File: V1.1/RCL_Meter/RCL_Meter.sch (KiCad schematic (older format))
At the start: 12 parts

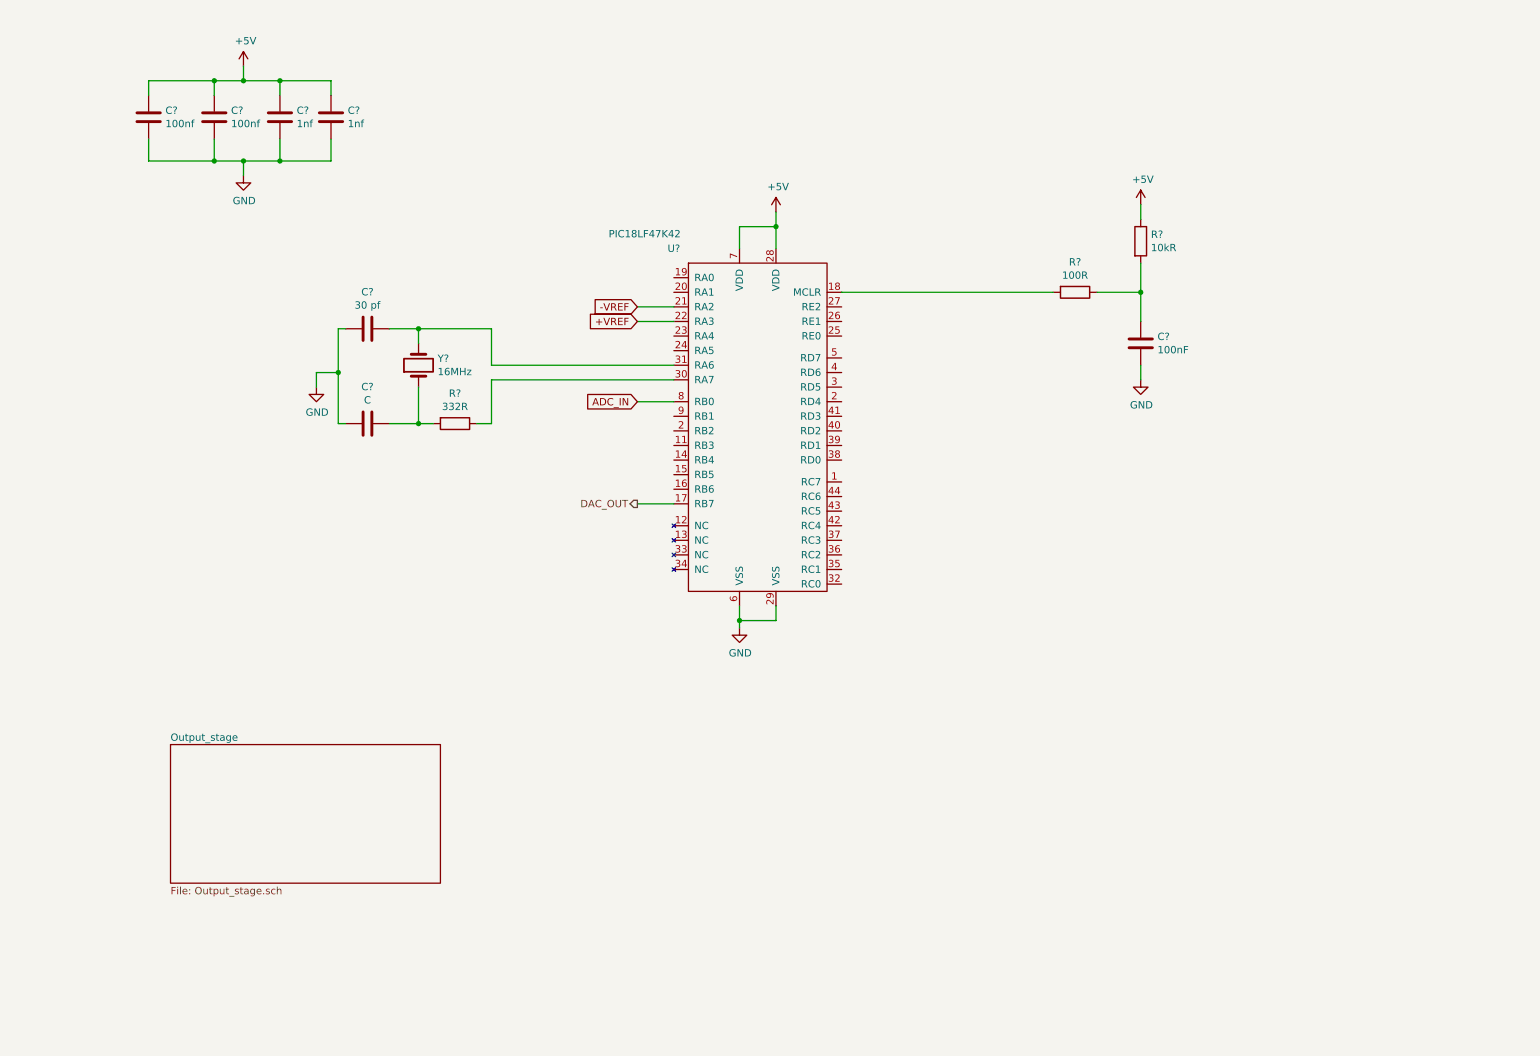
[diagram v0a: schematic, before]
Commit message: Added voltage and current front end
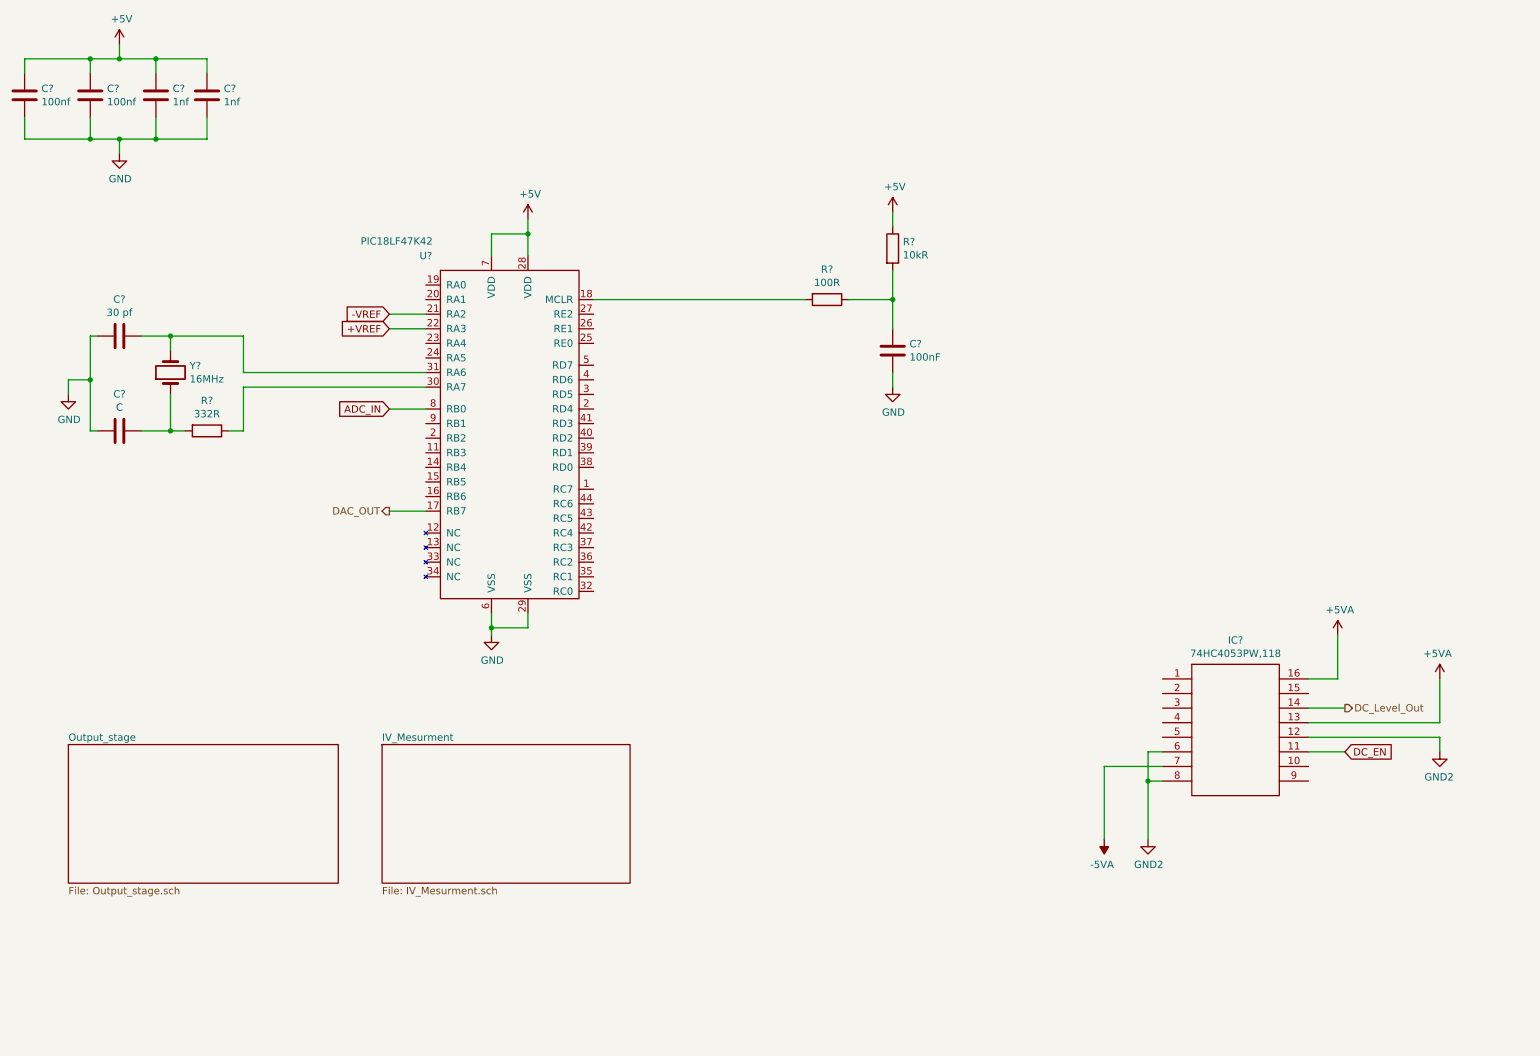
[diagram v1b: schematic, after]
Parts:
- added IC?: 74HC4053PW,118, SOP65P640X110-16N, symbol 74HC4053PW_118:74HC4053PW,118
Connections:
- new net +5VA: IC?.13, IC?.16
- new net -5VA: IC?.7
- new net DC_EN: IC?.11
- new net DC_Level_Out: IC?.14
- new net GND2: IC?.12, IC?.6, IC?.8
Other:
- moved on the sheet: C?, R?, U?, Y?

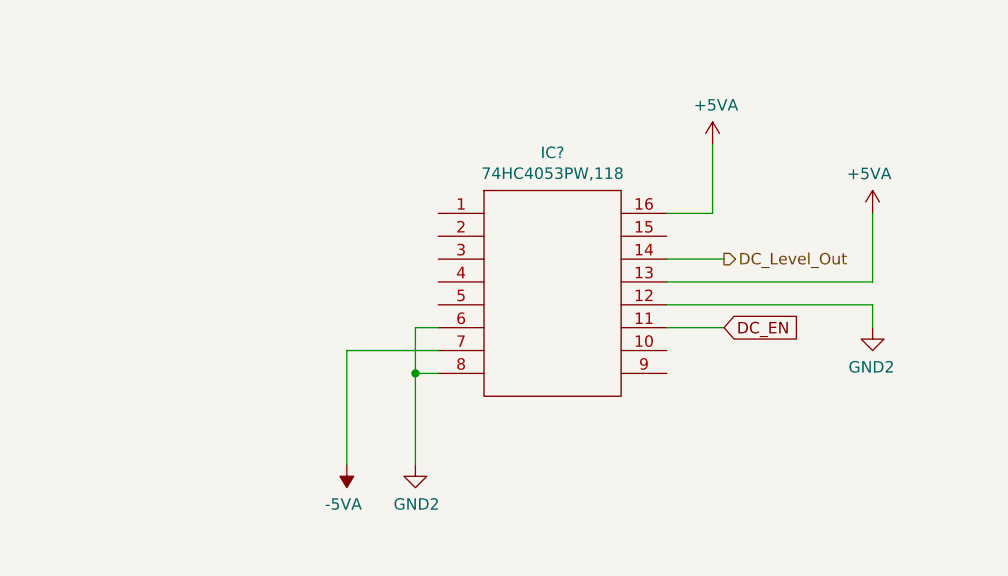
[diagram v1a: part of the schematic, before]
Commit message: added a PGA amplifier to instrumentation amplifier output
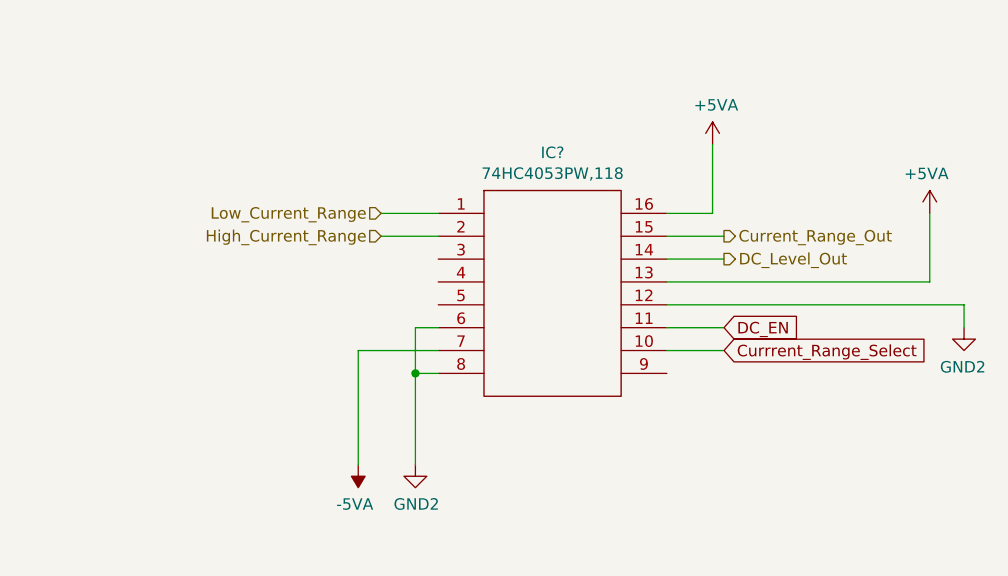
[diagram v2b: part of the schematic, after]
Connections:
- net Low_Current_Range: now reaches IC?.1
- net Currrent_Range_Select: now reaches IC?.10
- net Current_Range_Out: now reaches IC?.15
- net High_Current_Range: now reaches IC?.2
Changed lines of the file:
@@
 L power:-5VA #PWR?
 U 1 1 5F447F99
-P 8250 6200
-F 0 "#PWR?" H 8250 6300 50  0001 C CNN
-F 1 "-5VA" H 8265 6373 50  0000 C CNN
-F 2 "" H 8250 6200 50  0001 C CNN
-F 3 "" H 8250 6200 50  0001 C CNN
-	1    8250 6200
+P 8300 6200
+F 0 "#PWR?" H 8300 6300 50  0001 C CNN
+F 1 "-5VA" H 8315 6373 50  0000 C CNN
+F 2 "" H 8300 6200 50  0001 C CNN
+F 3 "" H 8300 6200 50  0001 C CNN
+	1    8300 6200
 	-1   0    0    1
 $EndComp
 Wire Wire Line
-	8250 6200 8250 5700
+	8300 6200 8300 5700
 Wire Wire Line
-	8250 5700 8650 5700
+	8300 5700 8650 5700
 Wire Wire Line
 	8550 5800 8550 5600
@@
 Connection ~ 8550 5800
 Wire Wire Line
-	10550 5400 10550 5100
+	10800 5400 10800 5100
 $Comp
 L power:+5VA #PWR?
 U 1 1 5F447FA5
-P 10550 5100
-F 0 "#PWR?" H 10550 4950 50  0001 C CNN
-F 1 "+5VA" H 10565 5273 50  0000 C CNN
-F 2 "" H 10550 5100 50  0001 C CNN
-F 3 "" H 10550 5100 50  0001 C CNN
-	1    10550 5100
+P 10800 5100
+F 0 "#PWR?" H 10800 4950 50  0001 C CNN
+F 1 "+5VA" H 10815 5273 50  0000 C CNN
+F 2 "" H 10800 5100 50  0001 C CNN
+F 3 "" H 10800 5100 50  0001 C CNN
+	1    10800 5100
 	-1   0    0    -1
 $EndComp
@@
 L power:GND2 #PWR?
 U 1 1 5F447FAB
-P 10550 5600
-F 0 "#PWR?" H 10550 5350 50  0001 C CNN
-F 1 "GND2" H 10555 5427 50  0000 C CNN
-F 2 "" H 10550 5600 50  0001 C CNN
-F 3 "" H 10550 5600 50  0001 C CNN
-	1    10550 5600
+P 10950 5600
+F 0 "#PWR?" H 10950 5350 50  0001 C CNN
+F 1 "GND2" H 10955 5427 50  0000 C CNN
+F 2 "" H 10950 5600 50  0001 C CNN
+F 3 "" H 10950 5600 50  0001 C CNN
+	1    10950 5600
 	-1   0    0    -1
 $EndComp
 Wire Wire Line
-	10550 5500 10550 5600
+	10950 5500 10950 5600
 Text GLabel 9900 5600 2    50   Input ~ 0
 DC_EN
@@
 Wire Wire Line
 	9900 5300 9650 5300
-Wire Wire Line
-	9650 5400 10550 5400
-Wire Wire Line
-	9650 5500 10550 5500
 $Sheet
 S 3300 5550 1700 950
@@
 F1 "IV_Mesurment.sch" 50
 $EndSheet
+Text HLabel 9900 5200 2    50   Output ~ 0
+Current_Range_Out
+Wire Wire Line
+	9650 5400 10800 5400
+Wire Wire Line
+	9900 5200 9650 5200
+Text HLabel 8400 5100 0    50   Input ~ 0
+Low_Current_Range
+Text HLabel 8400 5200 0    50   Input ~ 0
+High_Current_Range
+Wire Wire Line
+	8400 5100 8650 5100
+Wire Wire Line
+	8400 5200 8650 5200
+Text GLabel 9900 5700 2    50   Input ~ 0
+Currrent_Range_Select
+Wire Wire Line
+	9900 5700 9650 5700
+Wire Wire Line
+	9650 5500 10950 5500
 $EndSCHEMATC

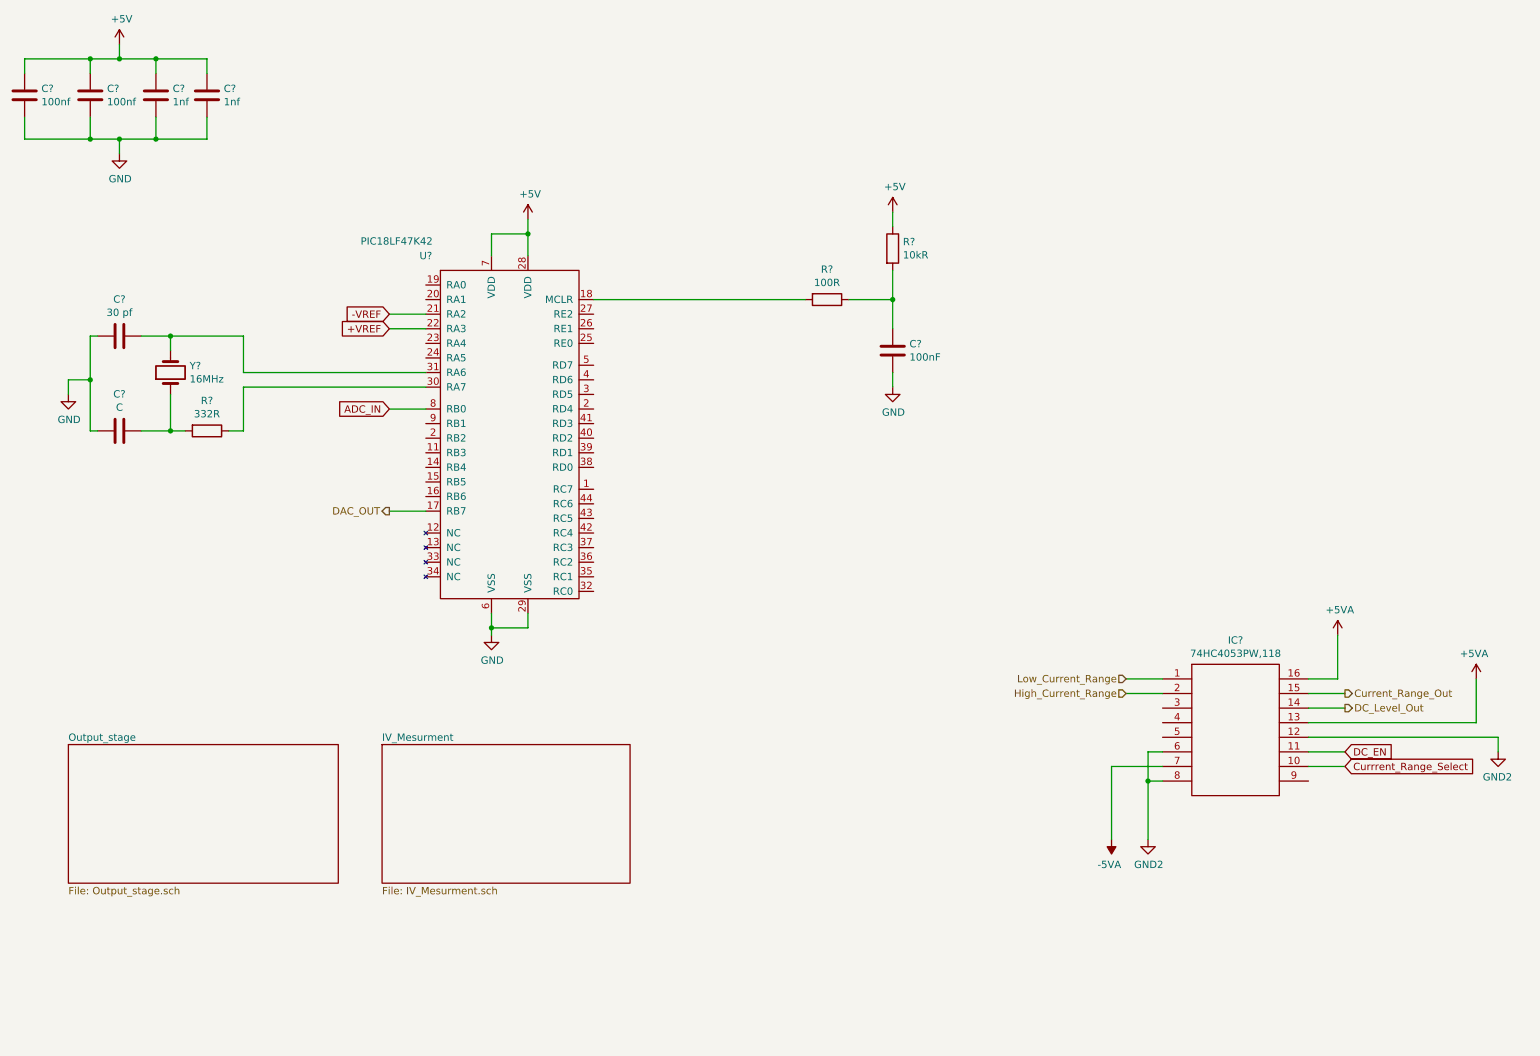
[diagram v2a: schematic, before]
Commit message: Created split power supply 12V to +-5V
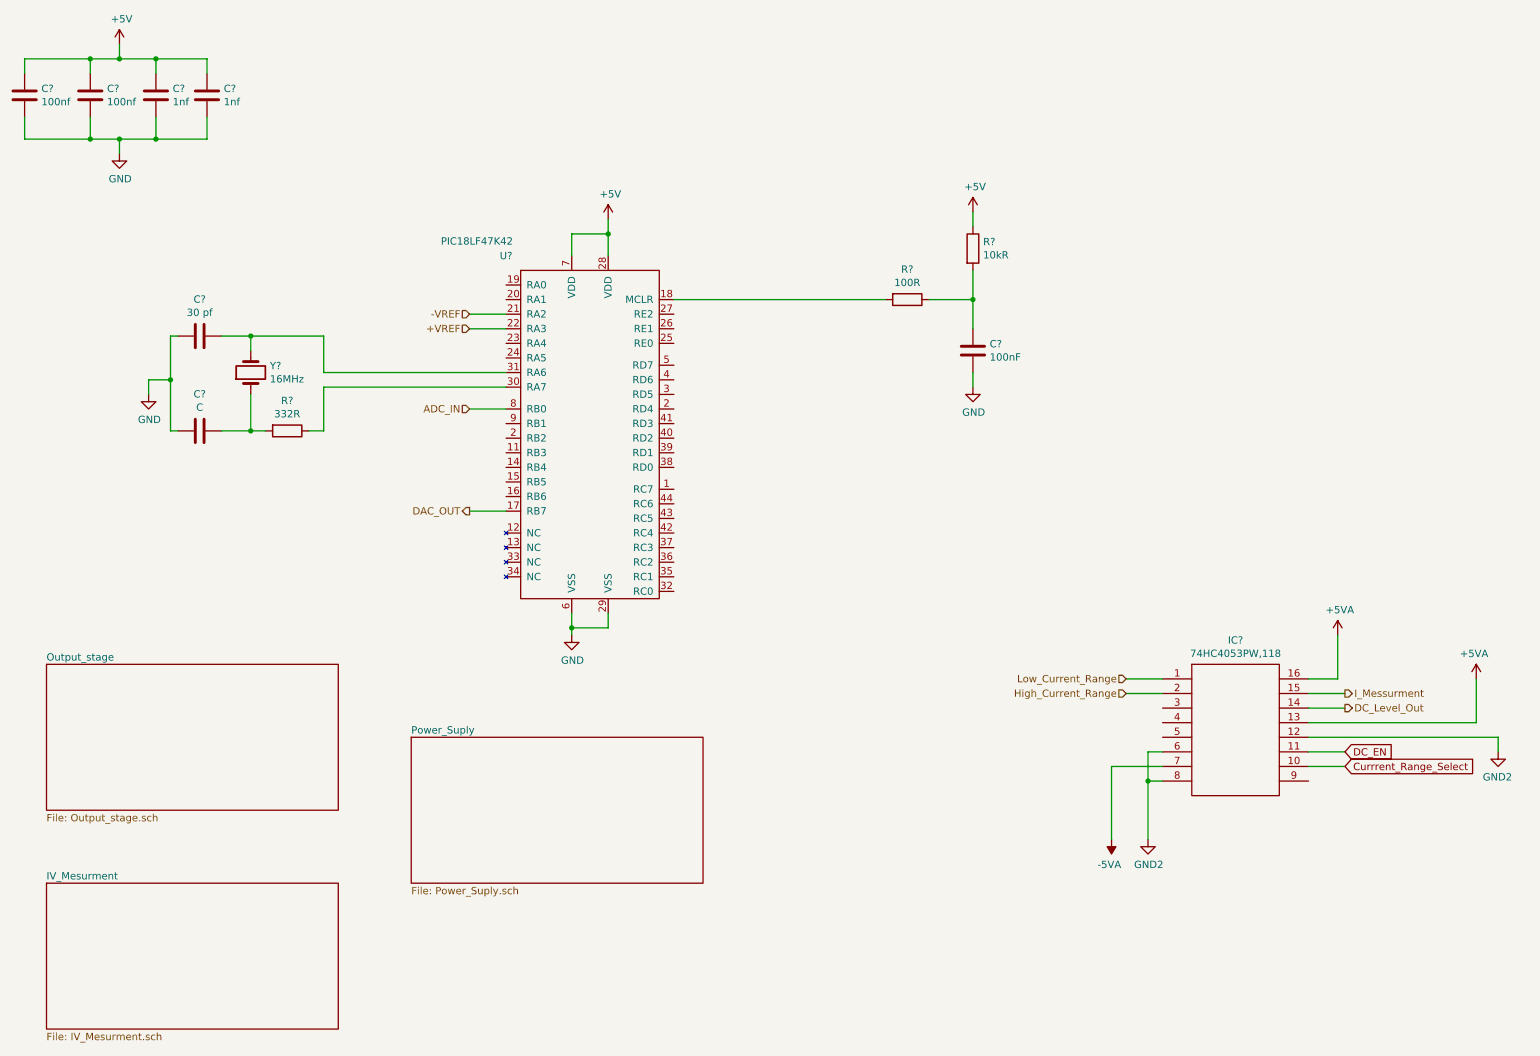
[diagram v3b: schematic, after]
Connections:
- net Current_Range_Out renamed I_Messurment
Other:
- moved on the sheet: C?, R?, U?, Y?
